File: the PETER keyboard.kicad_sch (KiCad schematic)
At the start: 140 parts, among them J1 USB_C_Receptacle_USB2.0, SW1 RotaryEncoder_Switch, SW12 RotaryEncoder_Switch, SW2 SW_Push, U1 ATmega32U4-M, Y1 Crystal_GND24_Small

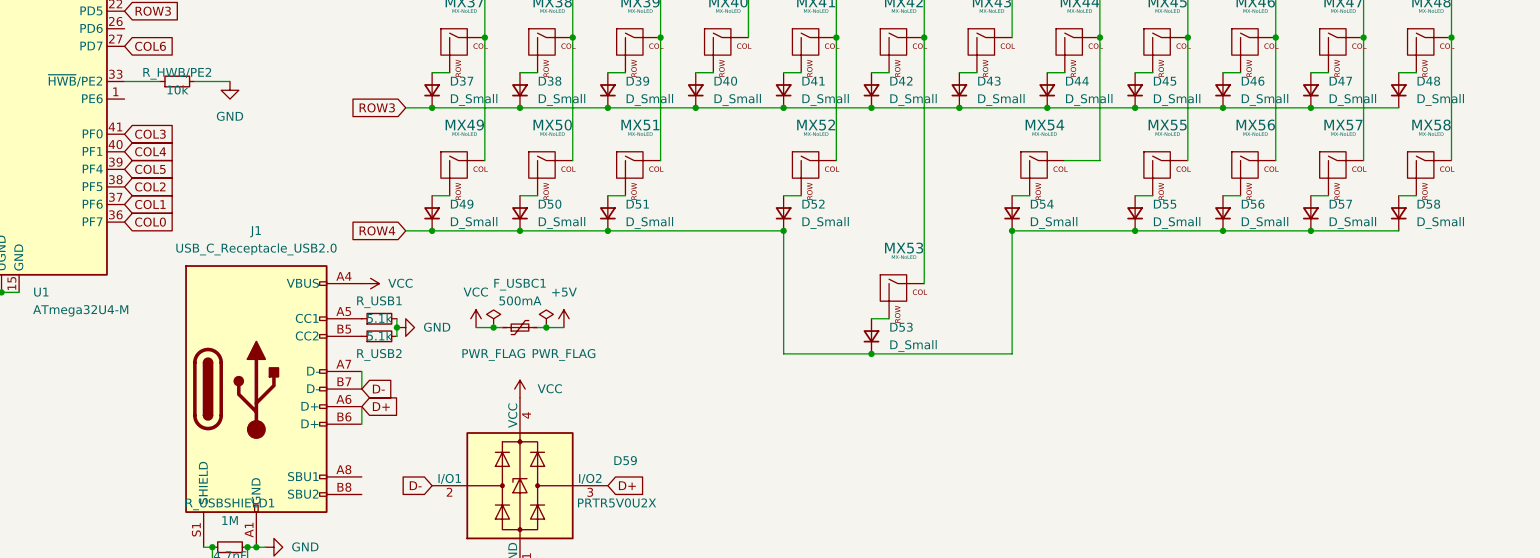
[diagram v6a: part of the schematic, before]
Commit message: rerouting, plate cuts
rerouted mcu, usb, all rows and cols. added plate cuts for bottom mounting
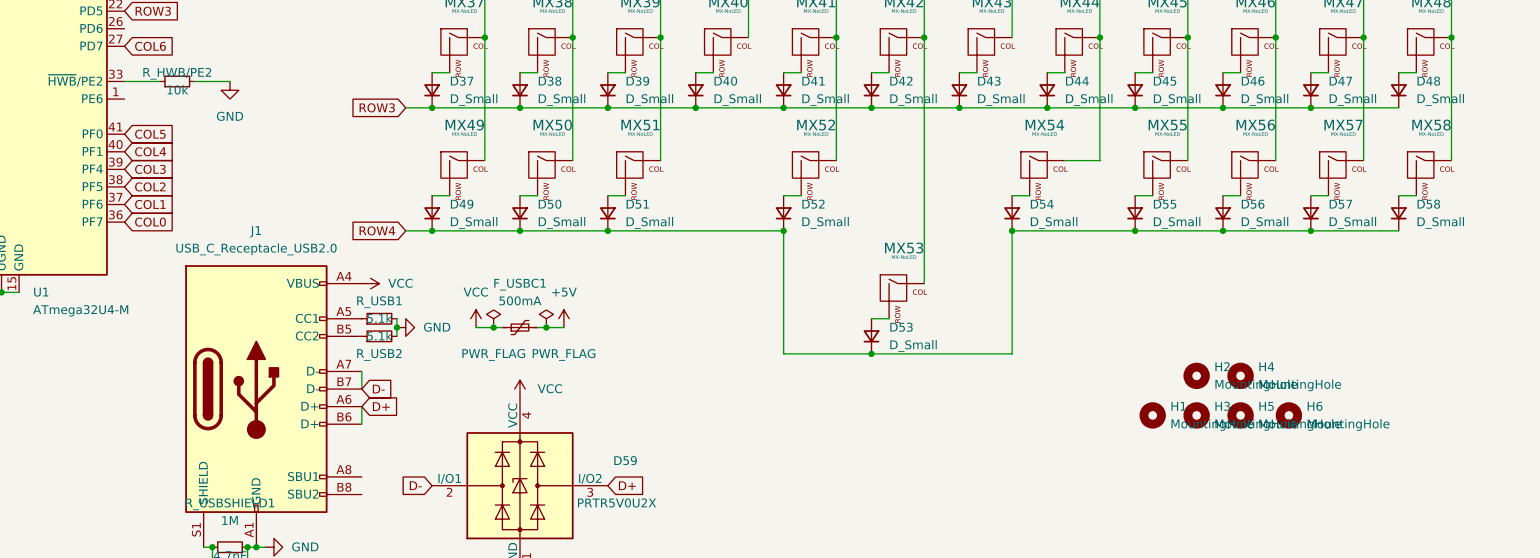
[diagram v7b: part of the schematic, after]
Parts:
- added H1, H2, H3, H4, H5, H6: MountingHole, MountingHole:MountingHole_2.2mm_M2, symbol Mechanical:MountingHole
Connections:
- net COL3: now also U1.39 (PF4); no longer U1.41 (PF0)
- net COL5: now also U1.41 (PF0); no longer U1.39 (PF4)
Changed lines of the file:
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@@
     )
   )
-  (global_label "COL3" (shape input) (at 60.96 92.71 0) (fields_autoplaced)
+  (global_label "COL3" (shape input) (at 60.96 97.79 0) (fields_autoplaced)
     (effects (font (size 1.27 1.27)) (justify left))
-    (property "Intersheet References" "${INTERSHEET_REFS}" (id 0) (at 68.2112 92.6306 0)
+    (property "Intersheet References" "${INTERSHEET_REFS}" (id 0) (at 68.2112 97.7106 0)
       (effects (font (size 1.27 1.27)) (justify left) hide)
     )
@@
     )
   )
-  (global_label "COL5" (shape input) (at 60.96 97.79 0) (fields_autoplaced)
+  (global_label "COL5" (shape input) (at 60.96 92.71 0) (fields_autoplaced)
     (effects (font (size 1.27 1.27)) (justify left))
-    (property "Intersheet References" "${INTERSHEET_REFS}" (id 0) (at 68.2112 97.7106 0)
+    (property "Intersheet References" "${INTERSHEET_REFS}" (id 0) (at 68.2112 92.6306 0)
       (effects (font (size 1.27 1.27)) (justify left) hide)
     )
@@
     (pin "2")
   )
+  (symbol (lib_id "Mechanical:MountingHole") (at 222.25 133.35 0) (unit 1)
+    (in_bom yes) (on_board yes) (fields_autoplaced)
+    (property "Reference" "H5" (id 0) (at 224.79 132.0799 0)
+      (effects (font (size 1.27 1.27)) (justify left))
+    )
+    (property "Value" "MountingHole" (id 1) (at 224.79 134.6199 0)
+      (effects (font (size 1.27 1.27)) (justify left))
+    )
+    (property "Footprint" "MountingHole:MountingHole_2.2mm_M2" (id 2) (at 222.25 133.35 0)
+      (effects (font (size 1.27 1.27)) hide)
+    )
+    (property "Datasheet" "~" (id 3) (at 222.25 133.35 0)
+      (effects (font (size 1.27 1.27)) hide)
+    )
+  )
   (symbol (lib_id "MX_Alps_Hybrid:MX-NoLED") (at 160.02 44.45 0) (unit 1)
     (in_bom yes) (on_board yes) (fields_autoplaced)
@@
     (pin "2")
   )
+  (symbol (lib_id "Mechanical:MountingHole") (at 229.235 133.35 0) (unit 1)
+    (in_bom yes) (on_board yes) (fields_autoplaced)
+    (property "Reference" "H6" (id 0) (at 231.775 132.0799 0)
+      (effects (font (size 1.27 1.27)) (justify left))
+    )
+    (property "Value" "MountingHole" (id 1) (at 231.775 134.6199 0)
+      (effects (font (size 1.27 1.27)) (justify left))
+    )
+    (property "Footprint" "MountingHole:MountingHole_2.2mm_M2" (id 2) (at 229.235 133.35 0)
+      (effects (font (size 1.27 1.27)) hide)
+    )
+    (property "Datasheet" "~" (id 3) (at 229.235 133.35 0)
+      (effects (font (size 1.27 1.27)) hide)
+    )
+  )
   (symbol (lib_id "Device:R_Small") (at 76.2 152.4 90) (unit 1)
     (in_bom yes) (on_board yes) (fields_autoplaced)
@@
     (pin "2")
   )
+  (symbol (lib_id "Mechanical:MountingHole") (at 222.25 127.635 0) (unit 1)
+    (in_bom yes) (on_board yes) (fields_autoplaced)
+    (property "Reference" "H4" (id 0) (at 224.79 126.3649 0)
+      (effects (font (size 1.27 1.27)) (justify left))
+    )
+    (property "Value" "MountingHole" (id 1) (at 224.79 128.9049 0)
+      (effects (font (size 1.27 1.27)) (justify left))
+    )
+    (property "Footprint" "MountingHole:MountingHole_2.2mm_M2" (id 2) (at 222.25 127.635 0)
+      (effects (font (size 1.27 1.27)) hide)
+    )
+    (property "Datasheet" "~" (id 3) (at 222.25 127.635 0)
+      (effects (font (size 1.27 1.27)) hide)
+    )
+  )
   (symbol (lib_id "MX_Alps_Hybrid:MX-NoLED") (at 210.82 97.79 0) (unit 1)
     (in_bom yes) (on_board yes) (fields_autoplaced)
@@
     (pin "2")
   )
+  (symbol (lib_id "Mechanical:MountingHole") (at 215.9 133.35 0) (unit 1)
+    (in_bom yes) (on_board yes) (fields_autoplaced)
+    (property "Reference" "H3" (id 0) (at 218.44 132.0799 0)
+      (effects (font (size 1.27 1.27)) (justify left))
+    )
+    (property "Value" "MountingHole" (id 1) (at 218.44 134.6199 0)
+      (effects (font (size 1.27 1.27)) (justify left))
+    )
+    (property "Footprint" "MountingHole:MountingHole_2.2mm_M2" (id 2) (at 215.9 133.35 0)
+      (effects (font (size 1.27 1.27)) hide)
+    )
+    (property "Datasheet" "~" (id 3) (at 215.9 133.35 0)
+      (effects (font (size 1.27 1.27)) hide)
+    )
+  )
   (symbol (lib_id "Device:C_Small") (at 22.86 104.14 90) (unit 1)
     (in_bom yes) (on_board yes)
@@
     (pin "2")
   )
+  (symbol (lib_id "Mechanical:MountingHole") (at 209.55 133.35 0) (unit 1)
+    (in_bom yes) (on_board yes) (fields_autoplaced)
+    (property "Reference" "H1" (id 0) (at 212.09 132.0799 0)
+      (effects (font (size 1.27 1.27)) (justify left))
+    )
+    (property "Value" "MountingHole" (id 1) (at 212.09 134.6199 0)
+      (effects (font (size 1.27 1.27)) (justify left))
+    )
+    (property "Footprint" "MountingHole:MountingHole_2.2mm_M2" (id 2) (at 209.55 133.35 0)
+      (effects (font (size 1.27 1.27)) hide)
+    )
+    (property "Datasheet" "~" (id 3) (at 209.55 133.35 0)
+      (effects (font (size 1.27 1.27)) hide)
+    )
+  )
   (symbol (lib_id "MX_Alps_Hybrid:MX-NoLED") (at 198.12 44.45 0) (unit 1)
     (in_bom yes) (on_board yes) (fields_autoplaced)
@@
     (pin "2")
   )
+  (symbol (lib_id "Mechanical:MountingHole") (at 215.9 127.635 0) (unit 1)
+    (in_bom yes) (on_board yes) (fields_autoplaced)
+    (property "Reference" "H2" (id 0) (at 218.44 126.3649 0)
+      (effects (font (size 1.27 1.27)) (justify left))
+    )
+    (property "Value" "MountingHole" (id 1) (at 218.44 128.9049 0)
+      (effects (font (size 1.27 1.27)) (justify left))
+    )
+    (property "Footprint" "MountingHole:MountingHole_2.2mm_M2" (id 2) (at 215.9 127.635 0)
+      (effects (font (size 1.27 1.27)) hide)
+    )
+    (property "Datasheet" "~" (id 3) (at 215.9 127.635 0)
+      (effects (font (size 1.27 1.27)) hide)
+    )
+  )
   (symbol (lib_id "power:+5V") (at 43.18 21.59 0) (unit 1)
     (in_bom yes) (on_board yes) (fields_autoplaced)
@@
       (reference "F_USBC1") (unit 1) (value "500mA") (footprint "Fuse:Fuse_1206_3216Metric")
     )
+    (path "/c583795e-c3ae-46d7-b825-5c0b3c80eabf"
+      (reference "H1") (unit 1) (value "MountingHole") (footprint "MountingHole:MountingHole_2.2mm_M2")
+    )
+    (path "/d188410f-33e9-458a-934f-d794e127fd5f"
+      (reference "H2") (unit 1) (value "MountingHole") (footprint "MountingHole:MountingHole_2.2mm_M2")
+    )
+    (path "/7822ac7f-08b7-44d3-a2fd-01a072b7afbd"
+      (reference "H3") (unit 1) (value "MountingHole") (footprint "MountingHole:MountingHole_2.2mm_M2")
+    )
+    (path "/4af30718-4865-49b3-a989-ec0ede27d553"
+      (reference "H4") (unit 1) (value "MountingHole") (footprint "MountingHole:MountingHole_2.2mm_M2")
+    )
+    (path "/1db0a83e-6411-45a6-876c-c0a8f9efcb45"
+      (reference "H5") (unit 1) (value "MountingHole") (footprint "MountingHole:MountingHole_2.2mm_M2")
+    )
+    (path "/32d9d407-7564-47af-b0db-4a8db137cdfe"
+      (reference "H6") (unit 1) (value "MountingHole") (footprint "MountingHole:MountingHole_2.2mm_M2")
+    )
     (path "/0628ca9e-38b0-425a-8423-920e559f6452"

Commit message: routing done
all routing done, curves added. 6u swapped for hotswap again. STABILIZERS NOT CHANGED YET
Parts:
- MX53: footprint MX_Only:MXOnly-6U-Centered-NoLED -> MX_Only:MXOnly-6U-Centered-Hotswap
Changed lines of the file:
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@@
       (effects (font (size 0.508 0.508)))
     )
-    (property "Footprint" "MX_Only:MXOnly-6U-Centered-NoLED" (id 2) (at 156.845 116.205 0)
+    (property "Footprint" "MX_Only:MXOnly-6U-Centered-Hotswap" (id 2) (at 156.845 116.205 0)
       (effects (font (size 1.524 1.524)) hide)
     )
@@
     )
     (path "/0870f4c6-cf74-4d41-94d2-7eecd22517a4"
-      (reference "MX53") (unit 1) (value "MX-NoLED") (footprint "MX_Only:MXOnly-6U-Centered-NoLED")
+      (reference "MX53") (unit 1) (value "MX-NoLED") (footprint "MX_Only:MXOnly-6U-Centered-Hotswap")
     )
     (path "/150cbac0-f7f3-42a2-9fee-ab866a5399d2"
